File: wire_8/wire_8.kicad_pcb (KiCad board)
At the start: 2 copper layers, 18.8 x 20.4 mm, 2 parts, among them J1 Moat_Wire_8, J2 Moat_Wire_12

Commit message: Wire 8 build
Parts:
- J1: footprint localstuff:Moat_16_2side_HS -> localstuff:Moat_8_2side_HSF
- moved J1 4.96 mm to (24.3, 56.7)
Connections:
- J1 pad 1: Net-(J1-Pad1) -> /GND
- J1 pad 2: Net-(J1-Pad2) -> /Bus1
- J1 pad 3: /5V -> /Bus2
- J1 pad 4: /12V -> /Bus3
- J1 pad 6: /GND -> /12V
- J1 pad 7: /Bus3 -> /24V
- J1 pad 8: /GND -> /GNDPWR
- J2 pad 11: Net-(J1-Pad1) -> unconnected-(J2-Pad11)
- J2 pad 12: Net-(J1-Pad2) -> unconnected-(J2-Pad12)
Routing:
- net /GND: track 40.8 -> 16.4 mm, vias 18 -> 6
- net /24V: track 34.6 -> 11.2 mm, vias 1 -> 0
- net /GNDPWR: track 37.6 -> 15.7 mm, vias 2 -> 0
- net Net-(J1-Pad2): track 17.6 -> 0.00 mm, vias 2 -> 0
- net Net-(J1-Pad1): track 17.5 -> 0.00 mm, vias 1 -> 0
- net /Bus1: track 10.4 -> 16.1 mm
- net /12V: track 24.4 -> 19.7 mm
- net /5V: track 24.2 -> 20.4 mm, vias 3 -> 2
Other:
- board size 18.8 x 20.4 mm -> 18.8 x 13 mm
- board text added: "MoaT Wire 8"
- board text removed: "MoaT Wire 16"

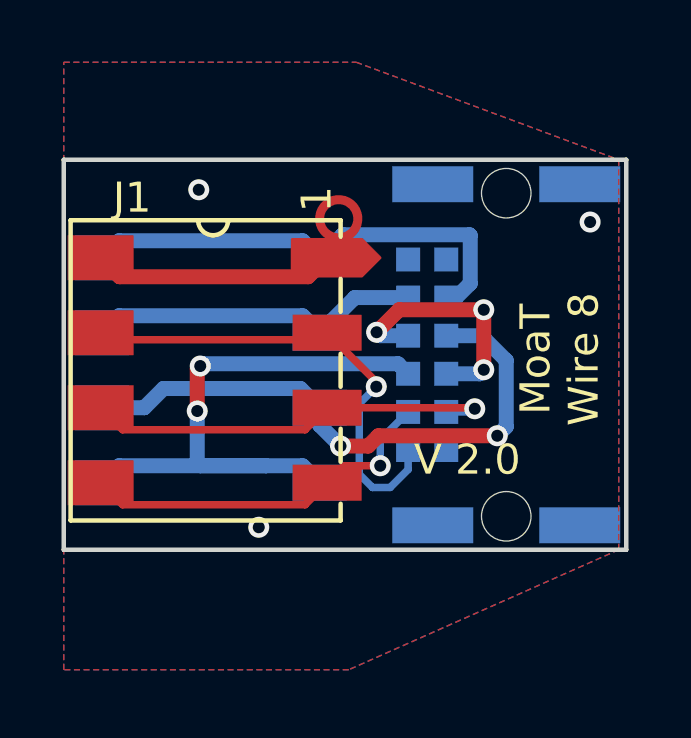
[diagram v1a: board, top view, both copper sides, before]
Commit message: Plug updates
drop in/out from plug24
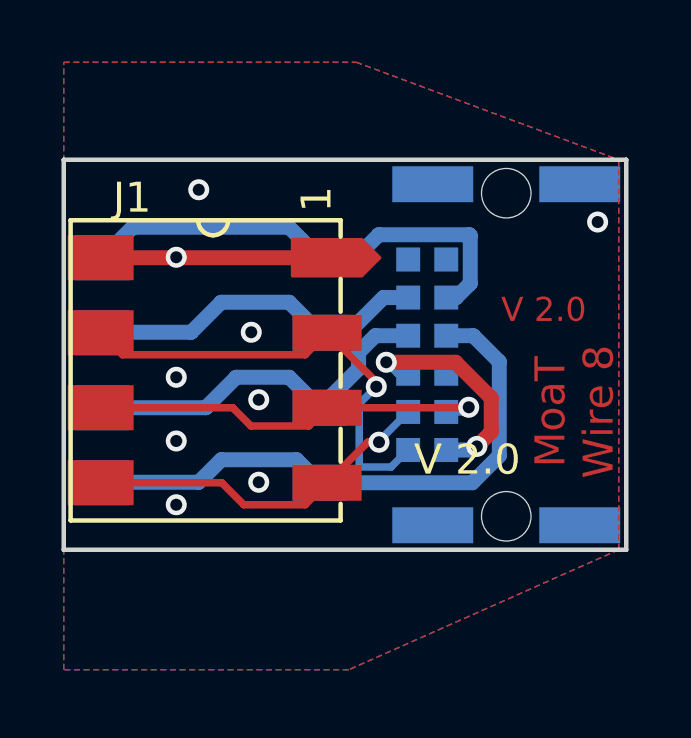
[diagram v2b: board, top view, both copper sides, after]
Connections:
- J2 pad 5: /GND -> unconnected-(J2-Pad5)
- J2 pad 6: /5V -> /GND
- J2 pad 7: /12V -> /5V
- J2 pad 8: /GND -> /12V
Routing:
- net /12V: track 19.7 -> 12.4 mm, vias 2 -> 0
- net /Bus1: track 16.1 -> 14.8 mm
- net /GND: track 16.4 -> 15.3 mm, vias 6 -> 11
- net /5V: track 20.4 -> 19.5 mm, vias 2 -> 0

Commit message: uploads
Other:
- board text added: "JLCJLCJLCJLC"
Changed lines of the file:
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@@
     (grid_origin 145 137.2)
     (pcbplotparams
-      (layerselection 0x0000008_7ffffffe)
+      (layerselection 0x00010f0_ffffffff)
       (disableapertmacros false)
       (usegerberextensions false)
@@
       (drillshape 0)
       (scaleselection 1)
-      (outputdirectory "")
+      (outputdirectory "gerber/")
     )
   )
@@
     (effects (font (size 1 1) (thickness 0.15)))
   )
+  (gr_text "JLCJLCJLCJLC" (at 37.1 52.05 90) (layer "B.SilkS")
+    (effects (font (size 1 1) (thickness 0.15)) (justify mirror))
+  )
   (gr_text "V 2.0" (at 32.7 54.7) (layer "F.SilkS")
